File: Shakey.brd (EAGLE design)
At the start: 146.4 x 62.1 mm, 81 parts, among them CN1 CONN_USB-4UCON-11071, U1 ATMEGA32U4-AU, U2 ICM-20689, U3 AP2210K-3.3TRG1, U4 LM75AD, Y1 16Mhz

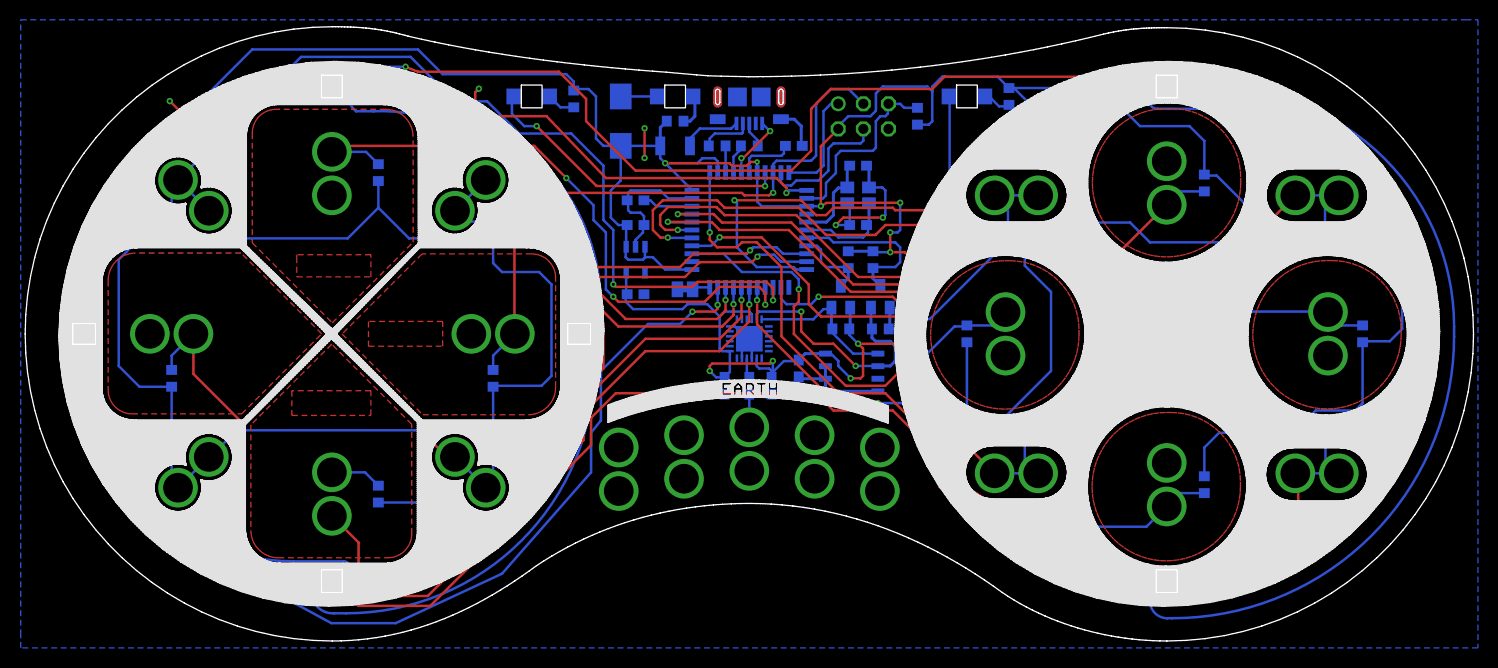
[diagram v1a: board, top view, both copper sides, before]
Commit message: added fiducial, branding text,logo
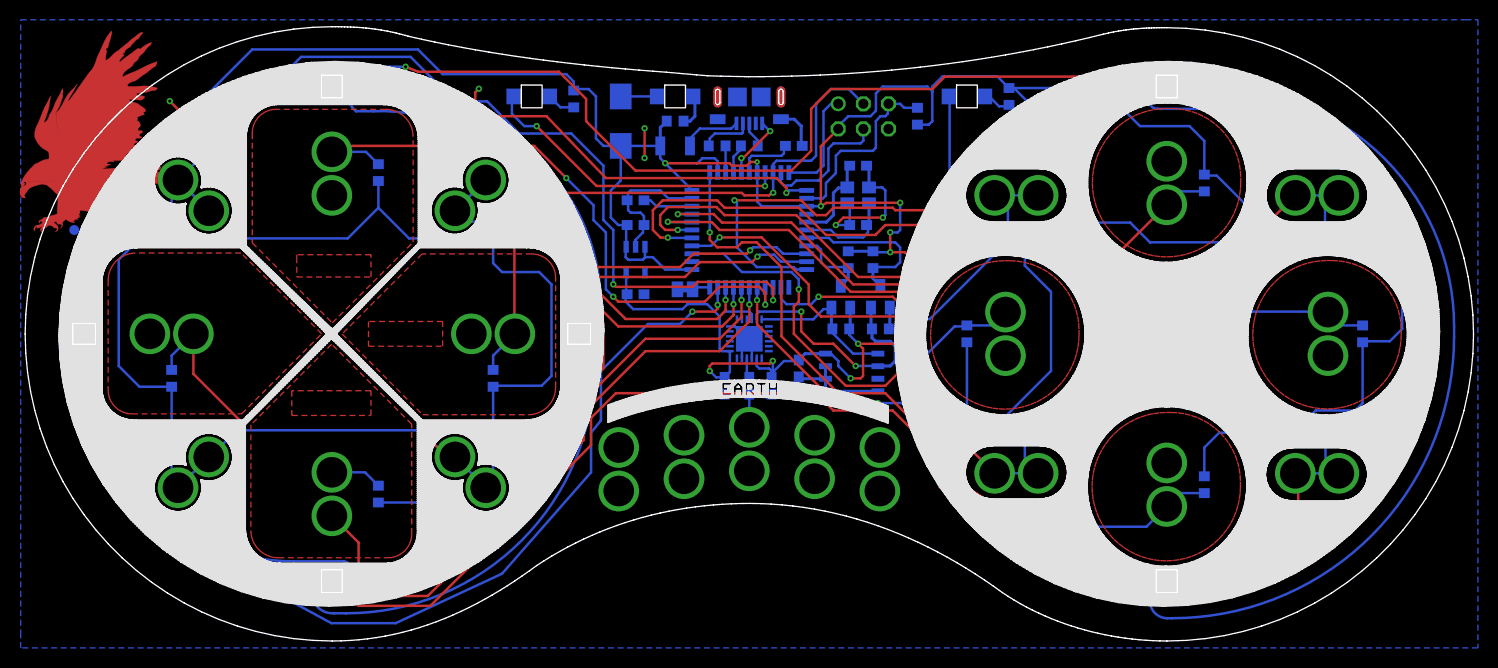
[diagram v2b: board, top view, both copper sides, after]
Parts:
- added U$7, U$8: FIDUCIAL-1X3MM, SixthLogic:FIDUCIAL-1X3MM
- added U$9: (no value), logo:EAGLE-TOP-15MM
- A, CLICK, DOWN, EARTH1, EARTH2, EARTH3, EARTH4, EARTH5, F, G, LEFT, MOUSE-DOWN, MOUSE-LEFT, MOUSE-LEFT-CLICK, MOUSE-RIGHT, MOUSE-RIGHT-CLICK, MOUSE-UP, RIGHT, SPACE, UP, W: device SixthLogic:MA01-1-ALLIGATOR-3MM -> SixthLogic:MA01-1-ALLIGATOR-3.1MM
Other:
- board text added: "Little Bird Co"
- board text added: "Manufactured in Australia"
- board text added: "SKU : LB-SHAKEY-1"
- board text added: "Shakey"
- board text added: "USB device for the WEB"
- board text added: "Version 1.0"
- board text added: "WebUSB"
- board text added: "by"

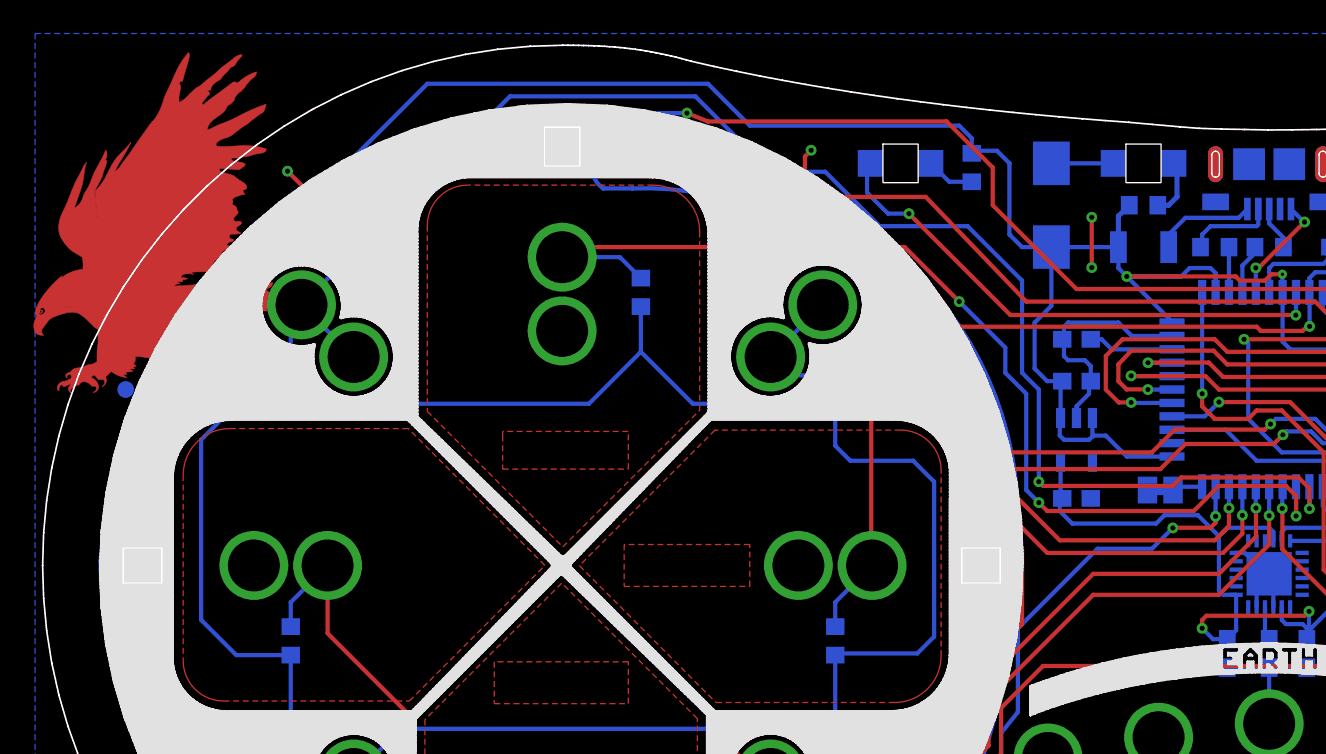
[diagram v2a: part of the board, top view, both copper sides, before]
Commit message: added Australian Made logo, adjusted some text to make them even
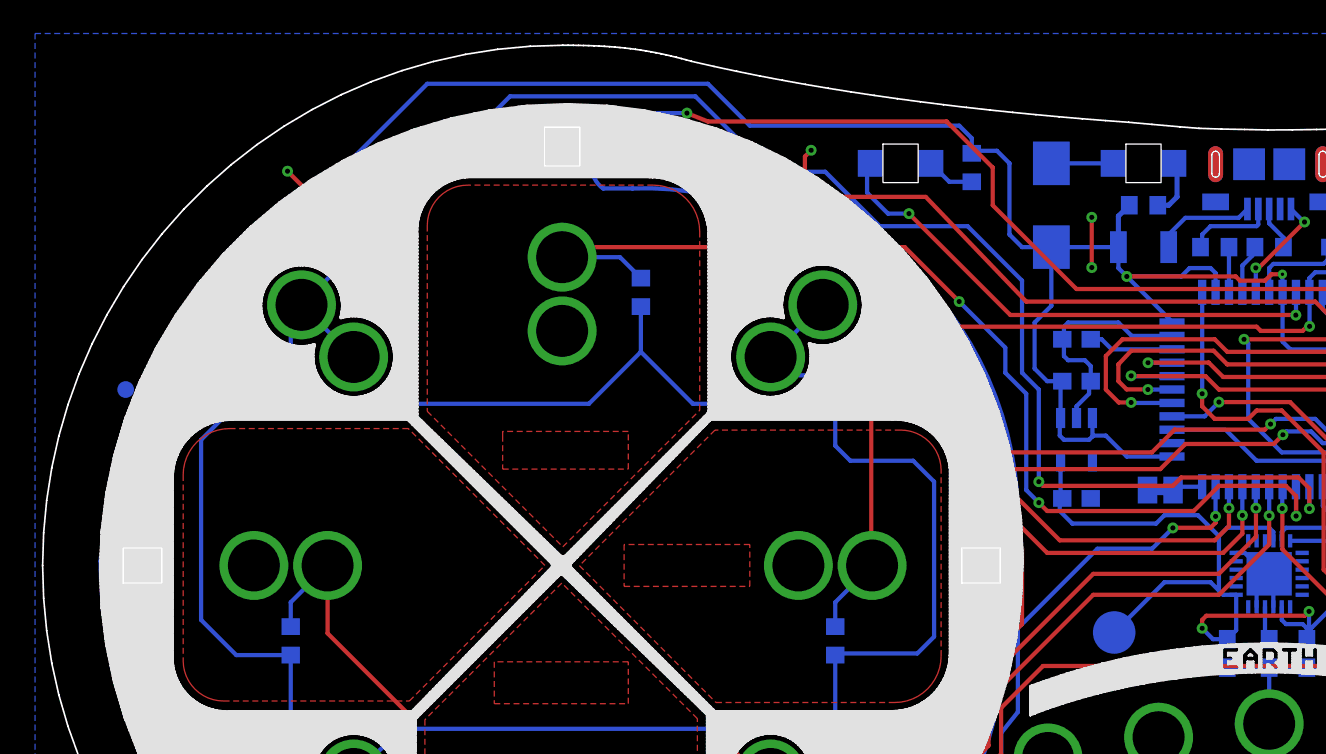
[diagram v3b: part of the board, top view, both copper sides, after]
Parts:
- removed U$9: (no value), logo:EAGLE-TOP-15MM
- added TP1: TPB2,54, testpad:B2,54
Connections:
- net 3.3V: now also TP1.TP
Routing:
- net 3.3V: track 66.1 -> 73.9 mm

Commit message: ready for production
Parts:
- removed U$7, U$8: FIDUCIAL-1X3MM, SixthLogic:FIDUCIAL-1X3MM
- added JP1, JP2: FIDUCIAL-1X3MM, SixthLogic:FIDUCIAL-1X3MM
- SJ1: value SOLDER JUMPER -> SOLDER_JUMPER
- TP1: value TPB2,54 -> TESTPAD; device testpad:B2,54 -> SixthLogic:TP-2.54MM
